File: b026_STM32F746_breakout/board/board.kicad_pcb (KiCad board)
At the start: 4 copper layers, 45 x 61 mm, 47 parts, among them J1 008_USB_2x2, J10 001_I2C_2x5, J11 002_SPI_2x5, J12 006_RMII_2x10, J13 Conn_01x02_Male, J14 012_CAN, J2 DebugEdge_02x05, J3 003_power_2x2, J4 010_UART, J5 007_ADC_2x5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

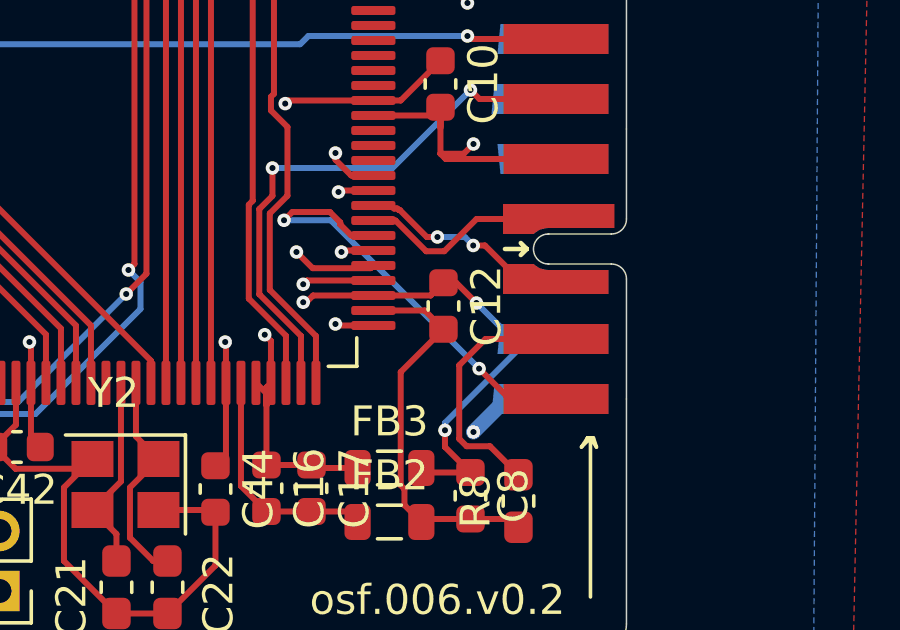
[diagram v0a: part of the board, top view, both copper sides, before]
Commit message: power and ground changed to higherarchial labels in subsheets
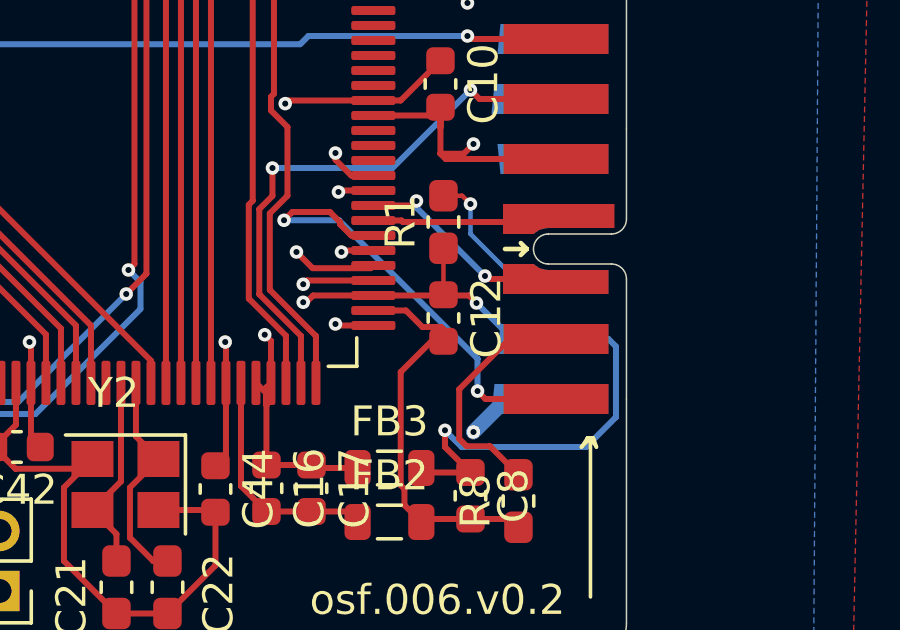
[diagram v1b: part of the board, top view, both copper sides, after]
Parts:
- added R1: 10k, Resistor_SMD:R_0603_1608Metric_Pad1.05x0.95mm_HandSolder, F.Cu at (115.9, 121.1)
- moved C12 0.40 mm to (115.9, 124.3)
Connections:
- net GNDA renamed /uC/GNDA
- J12 pad 18: (no net) -> Net-(J12-Pad18)
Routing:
- net +3V3: track 274.7 -> 281.7 mm
- net Net-(J12-Pad18): track 0.00 -> 5.74 mm, vias 0 -> 1
- net (no net): track 0.87 -> 0.00 mm
- net /uC/RXD0: track 5.71 -> 4.90 mm
- net /uC/CRS_DV: track 15.0 -> 15.6 mm
- net Net-(J11-Pad8): track 0.00 -> 0.57 mm
